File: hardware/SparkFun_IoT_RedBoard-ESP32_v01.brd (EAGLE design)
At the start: 68.6 x 58.4 mm, 212 parts, among them J1 5.5x2.1mm Barrel, J13 QWIIC_RIGHT_ANGLE, J15 MICRO-SD-PUSH-PUSH-EXT-PIN, J2 USB C, J3 USB_SOLDER_PADS, J5 M10NO_SILK, Q1 MBT3904DW1T1, Q11 20V/4.2A/52mΩ/1.4W, Q13 20V/4.2A/52mΩ/1.4W, Q3 20V/4.2A/52mΩ/1.4W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

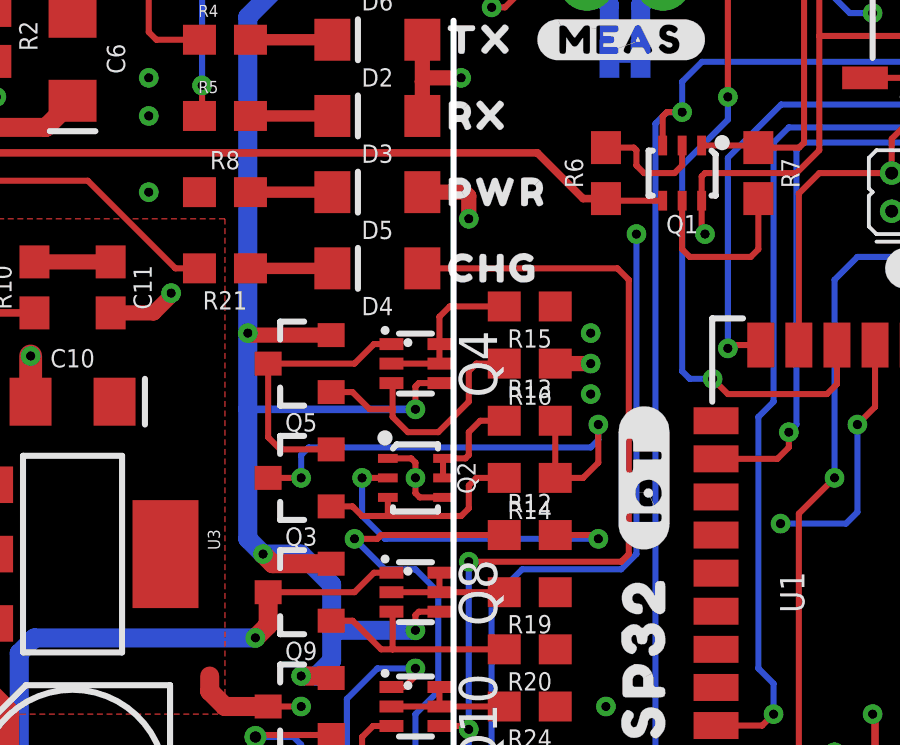
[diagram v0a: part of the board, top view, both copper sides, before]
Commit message: Flipped Q3, added 100R resistor to Q3's gate and changed panel to 2x2 boards
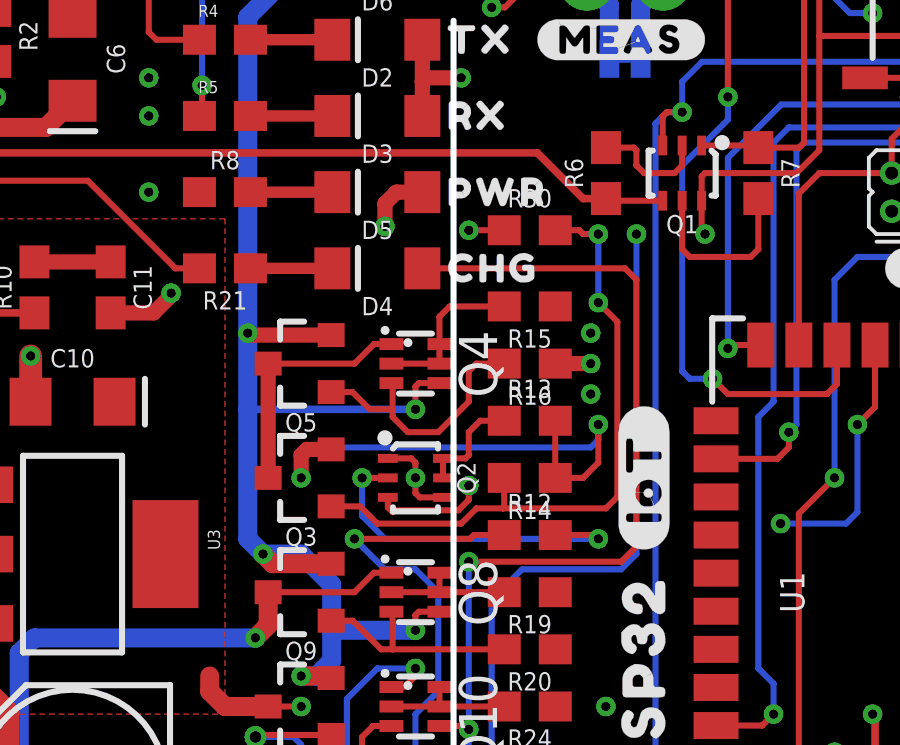
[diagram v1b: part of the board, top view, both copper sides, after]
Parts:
- added R30: 100, SparkFun-Resistors:0603
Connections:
- removed net N$19: Q2.3, Q3.1, R14.2
- new net N$11: Q2.3, R30.1
- new net N$9: Q3.1, R14.2, R30.2
- net VUSB_PROT: now also Q3.3; no longer Q3.2
- net V_USB: now also Q3.2; no longer Q3.3
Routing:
- net N$9: track 0.00 -> 21.7 mm, vias 0 -> 2
- net N$11: track 0.00 -> 13.4 mm, vias 0 -> 2
- net N$19: track 7.51 -> 0.00 mm
- net VUSB_PROT: track 9.10 -> 8.19 mm
- net V_USB: track 120.3 -> 121.0 mm
